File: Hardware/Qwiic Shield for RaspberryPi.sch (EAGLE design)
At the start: 22 parts, among them J1 Qwiic Right Angle, J6 Qwiic Right Angle, J7 Qwiic Right Angle, J8 Qwiic Right Angle, U2 3.3V/600mA, U3 RASPBERRY_PI

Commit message: Engineering checklist changes
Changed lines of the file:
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@@
 <instance part="FRAME1" gate="V" x="147.32" y="0"/>
 <instance part="LOGO1" gate="G$1" x="134.62" y="10.16"/>
-<instance part="FD1" gate="G$1" x="149.86" y="38.1"/>
-<instance part="FD2" gate="G$1" x="154.94" y="38.1"/>
+<instance part="FD1" gate="G$1" x="243.84" y="27.94"/>
+<instance part="FD2" gate="G$1" x="243.84" y="25.4"/>
 <instance part="J1" gate="G$1" x="205.74" y="149.86" smashed="yes" rot="MR180">
 <attribute name="VALUE" x="216.154" y="158.496" size="1.778" layer="96" font="vector" rot="MR0" align="top-left"/>
@@
 <instance part="SUPPLY8" gate="G$1" x="218.44" y="76.2"/>
 <instance part="GND8" gate="1" x="215.9" y="63.5"/>
-<instance part="FD3" gate="G$1" x="152.4" y="38.1"/>
-<instance part="FD4" gate="G$1" x="157.48" y="38.1"/>
+<instance part="FD3" gate="G$1" x="246.38" y="27.94"/>
+<instance part="FD4" gate="G$1" x="246.38" y="25.4"/>
 <instance part="LOGO2" gate="G$1" x="148.59" y="7.366"/>
 </instances>

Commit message: post design review
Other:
- note added: "V10"
- note removed: "V01"
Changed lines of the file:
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@@
 <text x="168.148" y="11.43" size="2.54" layer="94" font="vector">N. Seidle</text>
 <text x="38.1" y="160.02" size="3.048" layer="97" font="vector" ratio="12" align="center">Raspberry Pi</text>
-<text x="238.76" y="7.62" size="1.778" layer="94" font="vector" ratio="12">V01</text>
+<text x="238.76" y="7.62" size="1.778" layer="94" font="vector" ratio="12">V10</text>
 <text x="210.82" y="162.56" size="3.048" layer="97" font="vector" ratio="12" align="center">I2C Connections</text>
 <text x="96.52" y="160.02" size="3.048" layer="97" font="vector" ratio="12" align="center">Proto Connections</text>

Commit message: Updated PROD_ID of 2x20
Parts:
- U3: value RASPBERRY_PI -> RASPBERRY_PI_40BTM-NOHOLES
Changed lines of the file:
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@@
 <part name="U$1" library="SparkFun-Aesthetics" deviceset="SFE_LOGO_FLAME" device=".1_INCH"/>
 <part name="U$2" library="SparkFun-Aesthetics" deviceset="SFE_LOGO_NAME" device=".1_INCH" value="SFE_LOGO_NAME.1_INCH"/>
-<part name="U3" library="SparkFun-Connectors" deviceset="RASPBERRY_PI_40" device="BTM-NOHOLES" value="RASPBERRY_PI"/>
+<part name="U3" library="SparkFun-Connectors" deviceset="RASPBERRY_PI_40" device="BTM-NOHOLES" value=""/>
 <part name="SUPPLY11" library="SparkFun-PowerSymbols" deviceset="5V" device=""/>
 <part name="GND21" library="SparkFun" deviceset="GND" device=""/>

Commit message: v20 Initial Commit
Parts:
- removed J12, J2: (no value), SparkFun-Connectors:CONN_021X02_NO_SILK
- removed J3, J5: (no value), SparkFun-Connectors:CONN_041X04_NO_SILK
- removed J4: (no value), SparkFun-Connectors:CONN_06NO_SILK_FEMALE_PTH
- removed LOGO1: OSHW-LOGOMINI, SparkFun-Aesthetics:OSHW-LOGOMINI
- removed U$1: SFE_LOGO_FLAME.1_INCH, SparkFun-Aesthetics:SFE_LOGO_FLAME.1_INCH
- removed U$2: SFE_LOGO_NAME.1_INCH, SparkFun-Aesthetics:SFE_LOGO_NAME.1_INCH
- removed U3: RASPBERRY_PI_40BTM-NOHOLES, SparkFun-Connectors:RASPBERRY_PI_40BTM-NOHOLES
- added H1, H2, H3, H4, H5, H6: STAND-OFFTIGHT, SparkFun-Hardware:STAND-OFFTIGHT
- added J10: RASPBERRYPI-40-PIN-GPIO_PTH_NO_SHROUD, SparkFun-Connectors:RASPBERRYPI-40-PIN-GPIO_PTH_NO_SHROUD
- added LOGO3: SFE_LOGO_NAME_FLAME.2_INCH, SparkFun-Aesthetics:SFE_LOGO_NAME_FLAME.2_INCH
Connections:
- removed net CS: J3.4, U3.CS/D8
- removed net D7: J4.1, U3.D7
- new net N$1: J10.3.3V@17
- new net N$2: J10.3.3V@1
- net 3.3V: no longer J5.2
- net 5V: now also J10.5V@2, J10.5V@4; no longer J5.1, U3.5V
- net D12: now also J10.GP12; no longer J4.2, U3.D12
- net D13: now also J10.GP13; no longer U3.D13
- net D16: now also J10.GP16; no longer J4.4, U3.D16
- net D17: now also J10.GP17; no longer U3.D17
- net D18: now also J10.GP18#; no longer U3.PCM_CLK/D18
- net D19: now also J10.GP19; no longer U3.D19
- net D20: now also J10.GP20; no longer J4.5, U3.D20
- net D21: now also J10.GP21; no longer J4.6, U3.D21
- net D22: now also J10.GP22; no longer U3.D22
- net D23: now also J10.GP23; no longer U3.D23
- net D24: now also J10.GP24; no longer U3.D24
- net D25: now also J10.GP25; no longer U3.D25
- net D26: now also J10.GP26; no longer U3.D26
- net D27: now also J10.GP27; no longer U3.D27
- net D4: now also J10.GP4; no longer U3.D4
- net D5: now also J10.GP5; no longer U3.D5
- net D6: now also J10.GP6; no longer J4.3, U3.D6
- net GND: now also J10.GND@14, J10.GND@20, J10.GND@25, J10.GND@30, J10.GND@34, J10.GND@39, J10.GND@6, J10.GND@9; no longer J5.3, J5.4, U3.GND
- net ID_SCL: now also J10.ID_SC; no longer U3.ID_SCL
- net ID_SDA: now also J10.ID_SD; no longer U3.ID_SDA
- net MISO: now also J10.MISO; no longer J3.2, U3.MISO/D9
- net MOSI: now also J10.MOSI; no longer J3.1, U3.MOSI/D10
- net RX: now also J10.RXI; no longer J2.2, U3.RX/D15
- net SCK: now also J10.SCLK; no longer J3.3, U3.SCK/D11
- net SCL: now also J10.SCL; no longer J12.2, U3.SCL/D3
- net SDA: now also J10.SDA; no longer J12.1, U3.SDA/D2
- net TX: now also J10.TXO; no longer J2.1, U3.TX/D14
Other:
- note added: "A. England/Elias Santistevan"
- note added: "Qwiic Connectors"
- note added: "Raspberry Pi Connector"
- note added: "V20"
- note removed: "A. England"
- note removed: "I2C Connections"
- note removed: "Proto Connections"
- note removed: "Raspberry Pi"
- note removed: "V10"
- moved on the sheet: C1, C3, J1, J6, J7, J8, U2

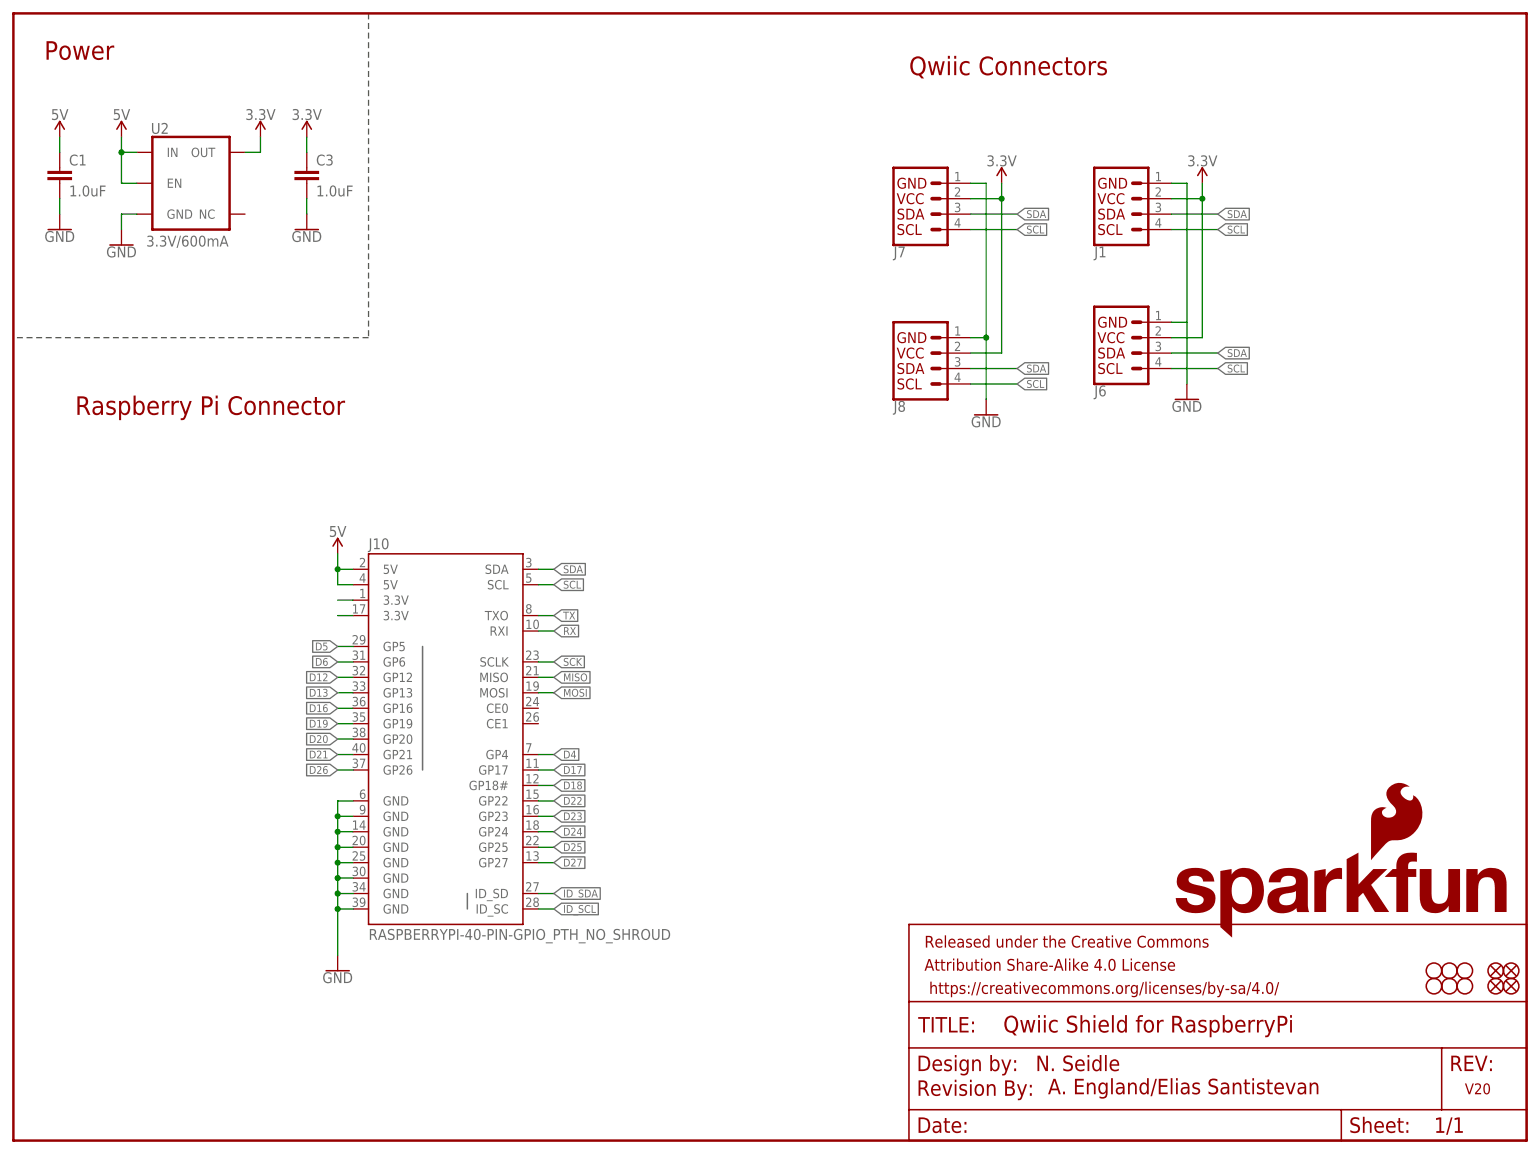
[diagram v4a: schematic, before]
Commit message: Updates silk
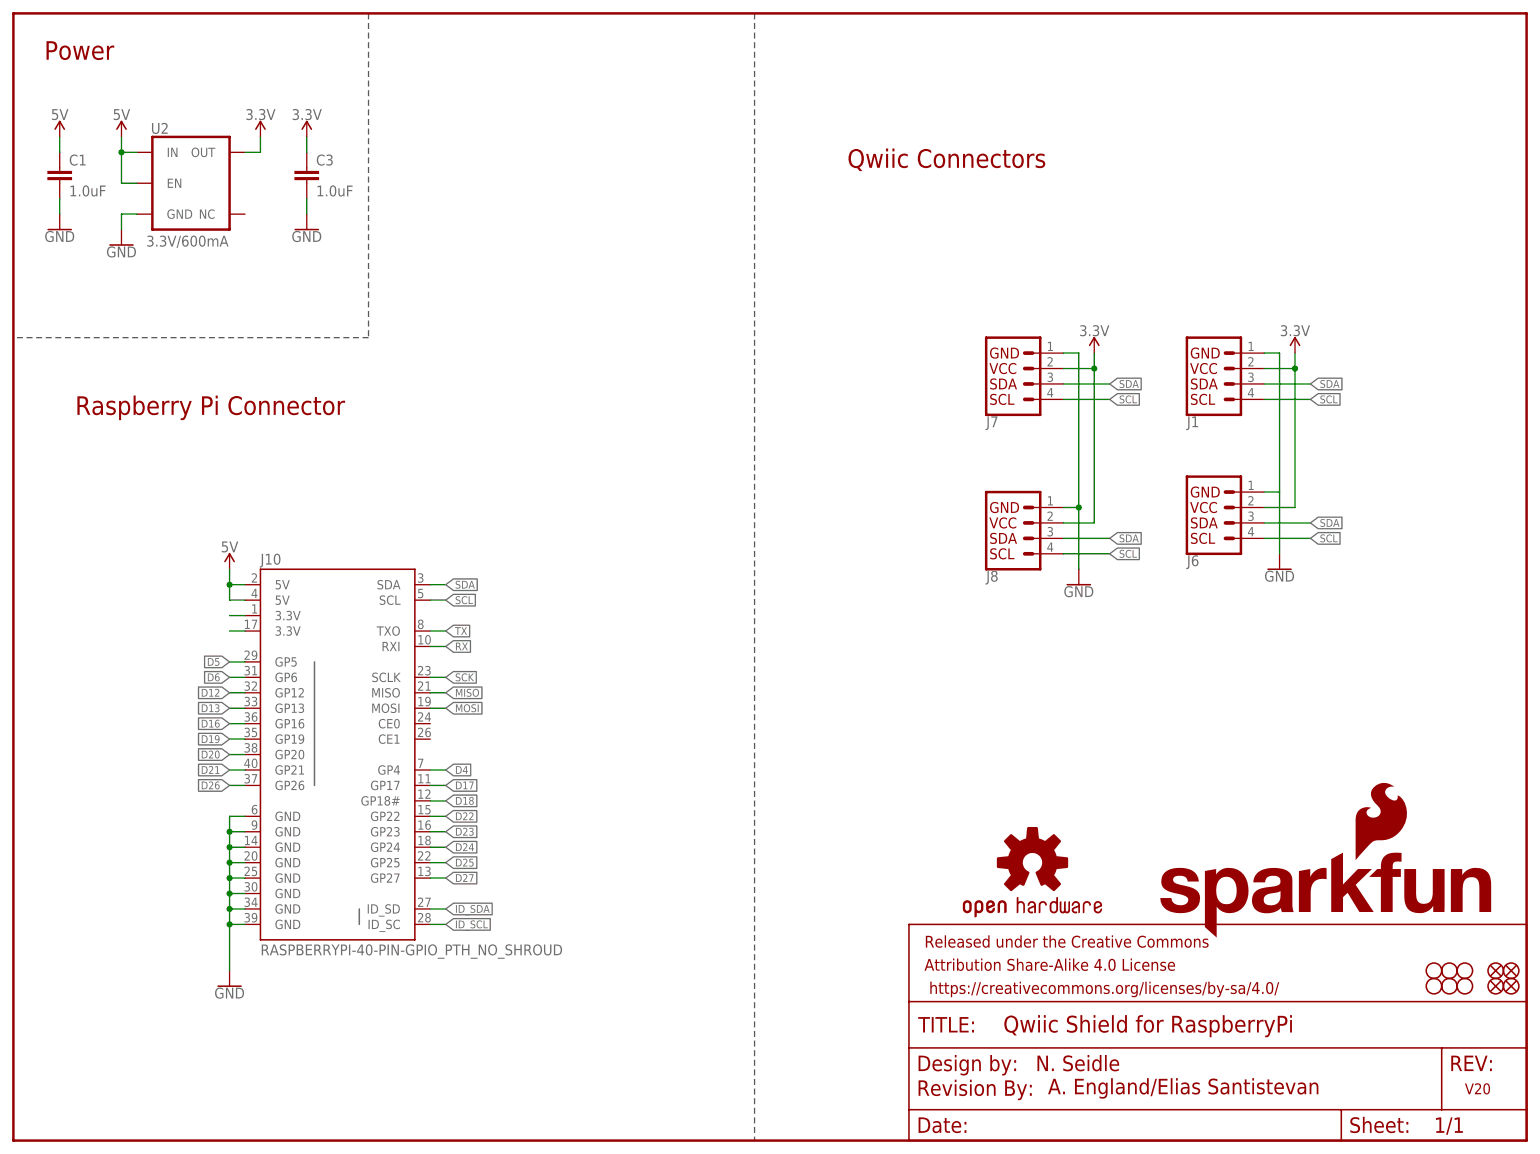
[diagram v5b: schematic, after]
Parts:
- added LOGO1: SFE_LOGO_NAME_FLAME.2_INCH, SparkFun-Aesthetics:SFE_LOGO_NAME_FLAME.2_INCH
- LOGO3: value SFE_LOGO_NAME_FLAME.2_INCH -> OSHW-LOGOS; device SparkFun-Aesthetics:SFE_LOGO_NAME_FLAME.2_INCH -> SparkFun-Aesthetics:OSHW-LOGOS
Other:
- moved on the sheet: J1, J10, J6, J7, J8

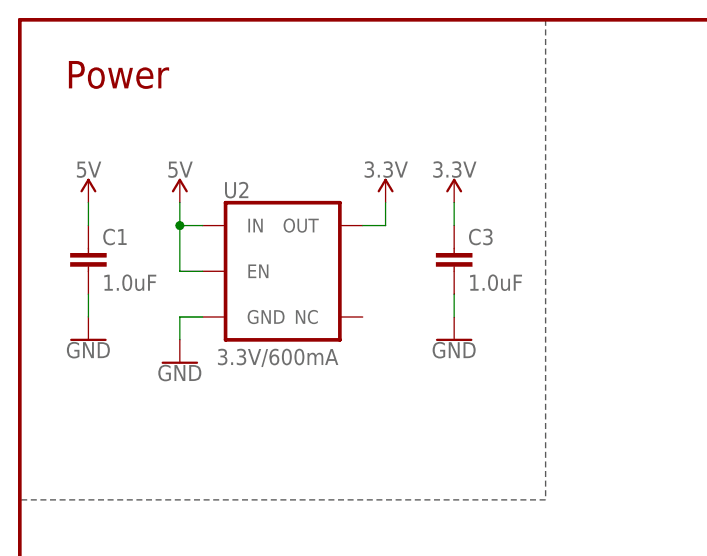
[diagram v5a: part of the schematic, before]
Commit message: Adjusts 1 inch spaced drill hits, adds seperation line to schematic
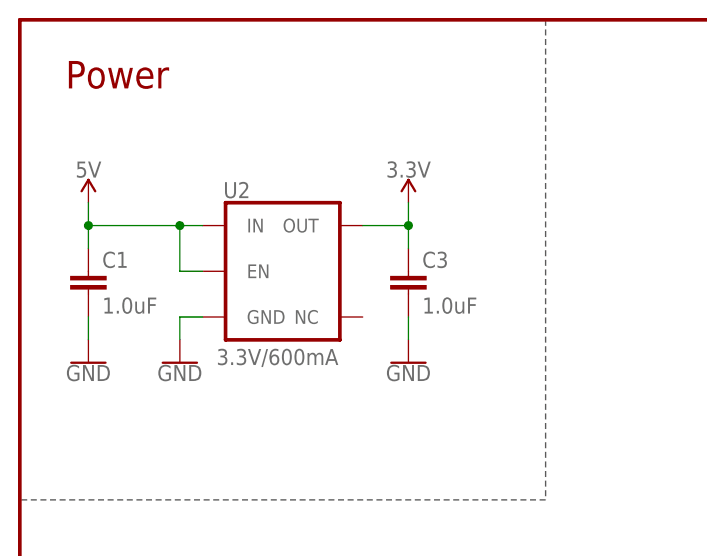
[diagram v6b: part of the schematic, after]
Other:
- moved on the sheet: C1, C3
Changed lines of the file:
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@@
 <part name="C1" library="SparkFun-Capacitors" deviceset="1.0UF" device="-0603-16V-10%" value="1.0uF"/>
 <part name="C3" library="SparkFun-Capacitors" deviceset="1.0UF" device="-0603-16V-10%" value="1.0uF"/>
-<part name="SUPPLY1" library="SparkFun-PowerSymbols" deviceset="5V" device=""/>
-<part name="SUPPLY2" library="SparkFun-PowerSymbols" deviceset="3.3V" device=""/>
 <part name="SUPPLY3" library="SparkFun-PowerSymbols" deviceset="3.3V" device=""/>
 <part name="SUPPLY4" library="SparkFun-PowerSymbols" deviceset="5V" device=""/>
@@
 <attribute name="VALUE" x="210.82" y="132.334" size="1.778" layer="96" align="bottom-center"/>
 </instance>
-<instance part="C1" gate="G$1" x="7.62" y="157.48" smashed="yes">
-<attribute name="NAME" x="9.144" y="160.401" size="1.778" layer="95" font="vector"/>
-<attribute name="VALUE" x="9.144" y="155.321" size="1.778" layer="96" font="vector"/>
-</instance>
-<instance part="C3" gate="G$1" x="48.26" y="157.48" smashed="yes">
-<attribute name="NAME" x="49.784" y="160.401" size="1.778" layer="95" font="vector"/>
-<attribute name="VALUE" x="49.784" y="155.321" size="1.778" layer="96" font="vector"/>
-</instance>
-<instance part="SUPPLY1" gate="G$1" x="17.78" y="165.1" smashed="yes">
-<attribute name="VALUE" x="17.78" y="167.894" size="1.778" layer="96" align="bottom-center"/>
-</instance>
-<instance part="SUPPLY2" gate="G$1" x="40.64" y="165.1" smashed="yes">
-<attribute name="VALUE" x="40.64" y="167.894" size="1.778" layer="96" align="bottom-center"/>
-</instance>
-<instance part="SUPPLY3" gate="G$1" x="48.26" y="165.1" smashed="yes">
-<attribute name="VALUE" x="48.26" y="167.894" size="1.778" layer="96" align="bottom-center"/>
+<instance part="C1" gate="G$1" x="7.62" y="154.94" smashed="yes">
+<attribute name="NAME" x="9.144" y="157.861" size="1.778" layer="95" font="vector"/>
+<attribute name="VALUE" x="9.144" y="152.781" size="1.778" layer="96" font="vector"/>
+</instance>
+<instance part="C3" gate="G$1" x="43.18" y="154.94" smashed="yes">
+<attribute name="NAME" x="44.704" y="157.861" size="1.778" layer="95" font="vector"/>
+<attribute name="VALUE" x="44.704" y="152.781" size="1.778" layer="96" font="vector"/>
+</instance>
+<instance part="SUPPLY3" gate="G$1" x="43.18" y="165.1" smashed="yes">
+<attribute name="VALUE" x="43.18" y="167.894" size="1.778" layer="96" align="bottom-center"/>
 </instance>
 <instance part="SUPPLY4" gate="G$1" x="7.62" y="165.1" smashed="yes">
@@
 <instance part="H5" gate="G$1" x="236.22" y="27.94" smashed="yes"/>
 <instance part="H6" gate="G$1" x="233.68" y="25.4" smashed="yes"/>
-<instance part="GND1" gate="1" x="7.62" y="149.86" smashed="yes">
-<attribute name="VALUE" x="7.62" y="149.606" size="1.778" layer="96" align="top-center"/>
+<instance part="GND1" gate="1" x="7.62" y="147.32" smashed="yes">
+<attribute name="VALUE" x="7.62" y="147.066" size="1.778" layer="96" align="top-center"/>
 </instance>
 <instance part="GND2" gate="1" x="17.78" y="147.32" smashed="yes">
 <attribute name="VALUE" x="17.78" y="147.066" size="1.778" layer="96" align="top-center"/>
 </instance>
-<instance part="GND3" gate="1" x="48.26" y="149.86" smashed="yes">
-<attribute name="VALUE" x="48.26" y="149.606" size="1.778" layer="96" align="top-center"/>
+<instance part="GND3" gate="1" x="43.18" y="147.32" smashed="yes">
+<attribute name="VALUE" x="43.18" y="147.066" size="1.778" layer="96" align="top-center"/>
 </instance>
 <instance part="LOGO1" gate="G$1" x="187.96" y="33.02" smashed="yes"/>
@@
 <segment>
 <pinref part="C1" gate="G$1" pin="2"/>
-<wire x1="7.62" y1="152.4" x2="7.62" y2="154.94" width="0.1524" layer="91"/>
+<wire x1="7.62" y1="149.86" x2="7.62" y2="152.4" width="0.1524" layer="91"/>
 <pinref part="GND1" gate="1" pin="GND"/>
 </segment>
@@
 <segment>
 <pinref part="C3" gate="G$1" pin="2"/>
-<wire x1="48.26" y1="154.94" x2="48.26" y2="152.4" width="0.1524" layer="91"/>
+<wire x1="43.18" y1="152.4" x2="43.18" y2="149.86" width="0.1524" layer="91"/>
 <pinref part="GND3" gate="1" pin="GND"/>
 </segment>
@@
 </segment>
 <segment>
-<wire x1="38.1" y1="162.56" x2="40.64" y2="162.56" width="0.1524" layer="91"/>
-<wire x1="40.64" y1="162.56" x2="40.64" y2="165.1" width="0.1524" layer="91"/>
-<pinref part="SUPPLY2" gate="G$1" pin="3.3V"/>
 <pinref part="U2" gate="G$1" pin="OUT"/>
-</segment>
-<segment>
 <pinref part="C3" gate="G$1" pin="1"/>
 <pinref part="SUPPLY3" gate="G$1" pin="3.3V"/>
-<wire x1="48.26" y1="162.56" x2="48.26" y2="165.1" width="0.1524" layer="91"/>
+<wire x1="43.18" y1="160.02" x2="43.18" y2="162.56" width="0.1524" layer="91"/>
+<wire x1="43.18" y1="162.56" x2="43.18" y2="165.1" width="0.1524" layer="91"/>
+<wire x1="38.1" y1="162.56" x2="43.18" y2="162.56" width="0.1524" layer="91"/>
+<junction x="43.18" y="162.56"/>
 </segment>
 <segment>
@@
 <net name="5V" class="0">
 <segment>
+<pinref part="C1" gate="G$1" pin="1"/>
+<pinref part="SUPPLY4" gate="G$1" pin="5V"/>
+<wire x1="7.62" y1="160.02" x2="7.62" y2="162.56" width="0.1524" layer="91"/>
+<wire x1="7.62" y1="162.56" x2="7.62" y2="165.1" width="0.1524" layer="91"/>
 <wire x1="20.32" y1="162.56" x2="17.78" y2="162.56" width="0.1524" layer="91"/>
-<wire x1="17.78" y1="162.56" x2="17.78" y2="165.1" width="0.1524" layer="91"/>
 <wire x1="20.32" y1="157.48" x2="17.78" y2="157.48" width="0.1524" layer="91"/>
 <wire x1="17.78" y1="157.48" x2="17.78" y2="162.56" width="0.1524" layer="91"/>
-<junction x="17.78" y="162.56"/>
-<pinref part="SUPPLY1" gate="G$1" pin="5V"/>
 <pinref part="U2" gate="G$1" pin="IN"/>
 <pinref part="U2" gate="G$1" pin="EN"/>
-</segment>
-<segment>
-<pinref part="C1" gate="G$1" pin="1"/>
-<pinref part="SUPPLY4" gate="G$1" pin="5V"/>
-<wire x1="7.62" y1="162.56" x2="7.62" y2="165.1" width="0.1524" layer="91"/>
-</segment>
-<segment>
+<wire x1="17.78" y1="162.56" x2="7.62" y2="162.56" width="0.1524" layer="91"/>
+<junction x="17.78" y="162.56"/>
+<junction x="7.62" y="162.56"/>
+</segment>
+<segment>
